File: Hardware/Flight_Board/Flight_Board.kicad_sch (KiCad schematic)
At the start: 0 parts

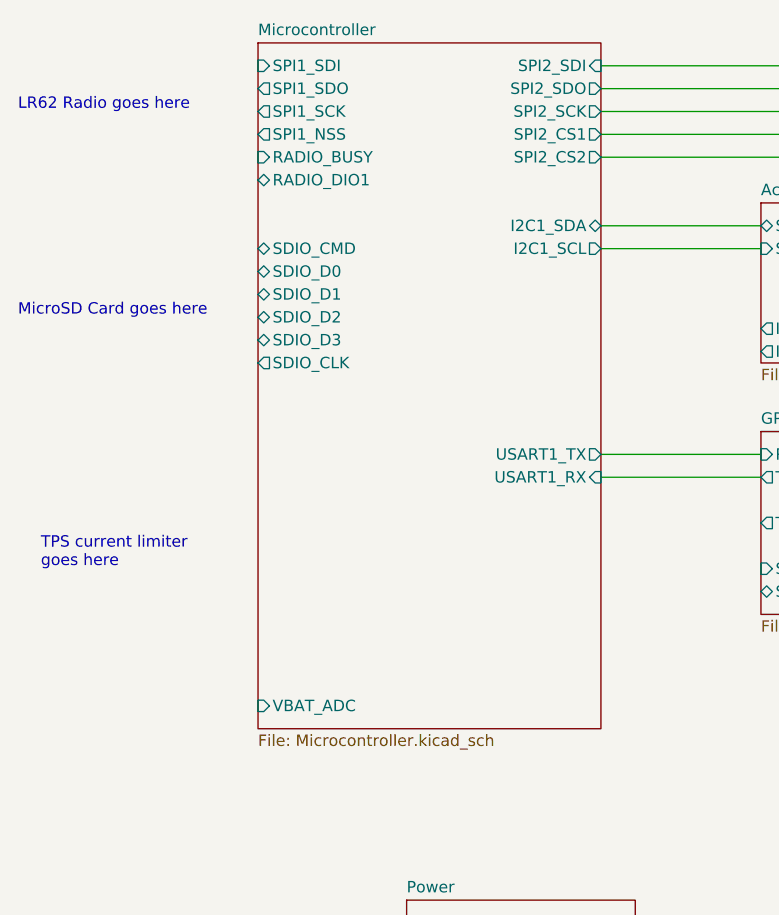
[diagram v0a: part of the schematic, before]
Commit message: add MicroSD
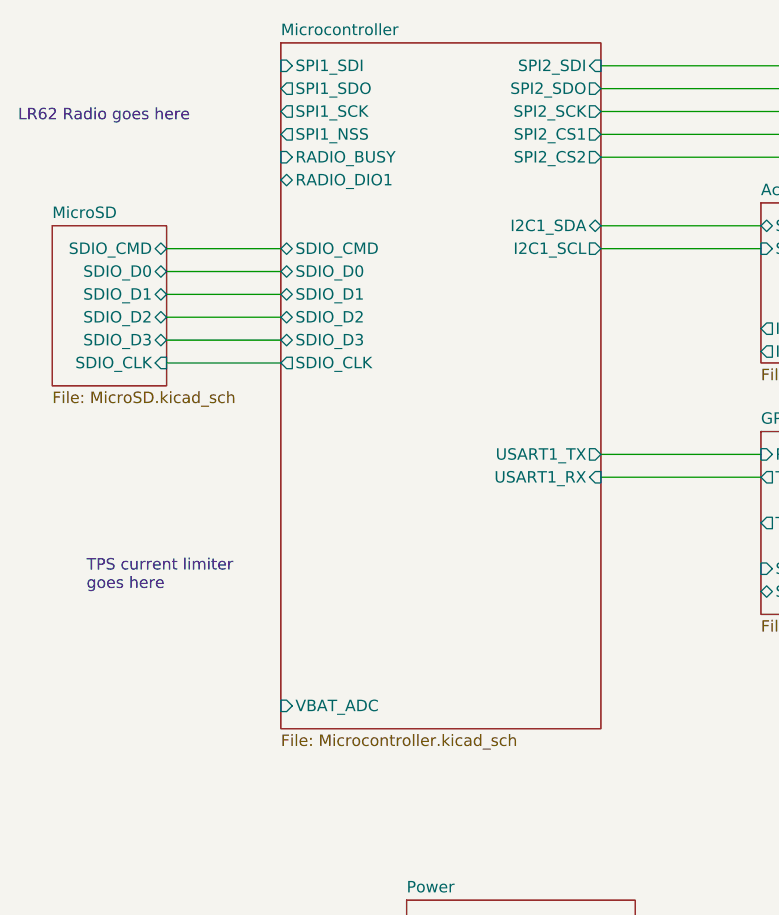
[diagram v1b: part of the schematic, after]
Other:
- added sheet MicroSD (MicroSD.kicad_sch)
- note removed: "MicroSD Card goes here"
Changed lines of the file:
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@@
+    (stroke (width 0) (type default))
+  )
+  (wire (pts (xy 127 60.96) (xy 139.7 60.96))
     (stroke (width 0) (type default))
   )
@@
     (stroke (width 0) (type default))
   )
+  (wire (pts (xy 127 68.58) (xy 139.7 68.58))
+    (stroke (width 0) (type default))
+  )
   (wire (pts (xy 233.68 68.58) (xy 238.76 68.58))
     (stroke (width 0) (type default))
@@
     (stroke (width 0) (type default))
   )
+  (wire (pts (xy 127 63.5) (xy 139.7 63.5))
+    (stroke (width 0) (type default))
+  )
   (wire (pts (xy 231.14 45.72) (xy 238.76 45.72))
     (stroke (width 0) (type default))
@@
     (stroke (width 0) (type default))
   )
+  (wire (pts (xy 127 73.66) (xy 139.7 73.66))
+    (stroke (width 0) (type default))
+  )
   (wire (pts (xy 233.68 43.18) (xy 233.68 68.58))
     (stroke (width 0) (type default))
@@
     (stroke (width 0) (type default))
   )
+  (wire (pts (xy 127 71.12) (xy 139.7 71.12))
+    (stroke (width 0) (type default))
+  )
   (wire (pts (xy 236.22 40.64) (xy 236.22 66.04))
     (stroke (width 0) (type default))
@@
     (stroke (width 0) (type default))
   )
+  (wire (pts (xy 127 66.04) (xy 139.7 66.04))
+    (stroke (width 0) (type default))
+  )
   (wire (pts (xy 175.26 58.42) (xy 193.04 58.42))
     (stroke (width 0) (type default))
@@
     (stroke (width 0) (type default))
   )
-  (text "MicroSD Card goes here" (at 110.49 68.58 0)
+  (text "TPS current limiter\ngoes here" (at 118.11 99.06 0)
     (effects (font (size 1.27 1.27)) (justify left bottom))
   )
-  (text "TPS current limiter\ngoes here" (at 113.03 96.52 0)
+  (text "LR62 Radio goes here" (at 110.49 46.99 0)
     (effects (font (size 1.27 1.27)) (justify left bottom))
   )
-  (text "LR62 Radio goes here" (at 110.49 45.72 0)
-    (effects (font (size 1.27 1.27)) (justify left bottom))
-  )
   (sheet (at 238.76 38.1) (size 12.7 17.78) (fields_autoplaced)
     (stroke (width 0.1524) (type solid))
@@
     )
   )
-  (sheet (at 137.16 38.1) (size 38.1 76.2) (fields_autoplaced)
-    (stroke (width 0.1524) (type solid))
-    (fill (color 0 0 0 0.0000))
-    (property "Sheetname" "Microcontroller" (at 137.16 37.3884 0)
-      (effects (font (size 1.27 1.27)) (justify left bottom))
-    )
-    (property "Sheetfile" "Microcontroller.kicad_sch" (at 137.16 114.8846 0)
+  (sheet (at 114.3 58.42) (size 12.7 17.78) (fields_autoplaced)
+    (stroke (width 0.1524) (type solid))
+    (fill (color 0 0 0 0.0000))
+    (property "Sheetname" "MicroSD" (at 114.3 57.7084 0)
+      (effects (font (size 1.27 1.27)) (justify left bottom))
+    )
+    (property "Sheetfile" "MicroSD.kicad_sch" (at 114.3 76.7846 0)
+      (effects (font (size 1.27 1.27)) (justify left top))
+    )
+    (pin "SDIO_D0" bidirectional (at 127 63.5 0)
+      (effects (font (size 1.27 1.27)) (justify right))
+    )
+    (pin "SDIO_D2" bidirectional (at 127 68.58 0)
+      (effects (font (size 1.27 1.27)) (justify right))
+    )
+    (pin "SDIO_D1" bidirectional (at 127 66.04 0)
+      (effects (font (size 1.27 1.27)) (justify right))
+    )
+    (pin "SDIO_D3" bidirectional (at 127 71.12 0)
+      (effects (font (size 1.27 1.27)) (justify right))
+    )
+    (pin "SDIO_CLK" input (at 127 73.66 0)
+      (effects (font (size 1.27 1.27)) (justify right))
+    )
+    (pin "SDIO_CMD" bidirectional (at 127 60.96 0)
+      (effects (font (size 1.27 1.27)) (justify right))
+    )
+    (instances
+      (project "Flight_Board"
+        (path "/e8eb85d5-f1ff-4500-895d-25b9ff5f6d36" (page "8"))
+      )
+    )
+  )
+  (sheet (at 139.7 38.1) (size 35.56 76.2) (fields_autoplaced)
+    (stroke (width 0.1524) (type solid))
+    (fill (color 0 0 0 0.0000))
+    (property "Sheetname" "Microcontroller" (at 139.7 37.3884 0)
+      (effects (font (size 1.27 1.27)) (justify left bottom))
+    )
+    (property "Sheetfile" "Microcontroller.kicad_sch" (at 139.7 114.8846 0)
       (effects (font (size 1.27 1.27)) (justify left top))
     )
@@
       (effects (font (size 1.27 1.27)) (justify right))
     )
-    (pin "SPI1_NSS" output (at 137.16 48.26 180)
-      (effects (font (size 1.27 1.27)) (justify left))
-    )
-    (pin "SPI1_SCK" output (at 137.16 45.72 180)
-      (effects (font (size 1.27 1.27)) (justify left))
-    )
-    (pin "SPI1_SDI" input (at 137.16 40.64 180)
-      (effects (font (size 1.27 1.27)) (justify left))
-    )
-    (pin "SPI1_SDO" output (at 137.16 43.18 180)
+    (pin "SPI1_NSS" output (at 139.7 48.26 180)
+      (effects (font (size 1.27 1.27)) (justify left))
+    )
+    (pin "SPI1_SCK" output (at 139.7 45.72 180)
+      (effects (font (size 1.27 1.27)) (justify left))
+    )
+    (pin "SPI1_SDI" input (at 139.7 40.64 180)
+      (effects (font (size 1.27 1.27)) (justify left))
+    )
+    (pin "SPI1_SDO" output (at 139.7 43.18 180)
       (effects (font (size 1.27 1.27)) (justify left))
     )
@@
       (effects (font (size 1.27 1.27)) (justify right))
     )
-    (pin "SDIO_CLK" output (at 137.16 73.66 180)
-      (effects (font (size 1.27 1.27)) (justify left))
-    )
-    (pin "RADIO_BUSY" input (at 137.16 50.8 180)
-      (effects (font (size 1.27 1.27)) (justify left))
-    )
-    (pin "RADIO_DIO1" bidirectional (at 137.16 53.34 180)
-      (effects (font (size 1.27 1.27)) (justify left))
-    )
-    (pin "SDIO_D3" bidirectional (at 137.16 71.12 180)
-      (effects (font (size 1.27 1.27)) (justify left))
-    )
-    (pin "SDIO_CMD" bidirectional (at 137.16 60.96 180)
-      (effects (font (size 1.27 1.27)) (justify left))
-    )
-    (pin "SDIO_D0" bidirectional (at 137.16 63.5 180)
-      (effects (font (size 1.27 1.27)) (justify left))
-    )
-    (pin "SDIO_D1" bidirectional (at 137.16 66.04 180)
-      (effects (font (size 1.27 1.27)) (justify left))
-    )
-    (pin "SDIO_D2" bidirectional (at 137.16 68.58 180)
-      (effects (font (size 1.27 1.27)) (justify left))
-    )
-    (pin "VBAT_ADC" input (at 137.16 111.76 180)
-      (effects (font (size 1.27 1.27)) (justify left))
-    )
+    (pin "SDIO_CLK" output (at 139.7 73.66 180)
+      (effects (font (size 1.27 1.27)) (justify left))
+    )
+    (pin "RADIO_BUSY" input (at 139.7 50.8 180)
+      (effects (font (size 1.27 1.27)) (justify left))
+    )
+    (pin "RADIO_DIO1" bidirectional (at 139.7 53.34 180)
+      (effects (font (size 1.27 1.27)) (justify left))
+    )
+    (pin "SDIO_D3" bidirectional (at 139.7 71.12 180)
+      (effects (font (size 1.27 1.27)) (justify left))
+    )
+    (pin "SDIO_CMD" bidirectional (at 139.7 60.96 180)
+      (effects (font (size 1.27 1.27)) (justify left))
+    )
+    (pin "SDIO_D0" bidirectional (at 139.7 63.5 180)
+      (effects (font (size 1.27 1.27)) (justify left))
+    )
+    (pin "SDIO_D1" bidirectional (at 139.7 66.04 180)
+      (effects (font (size 1.27 1.27)) (justify left))
+    )
+    (pin "SDIO_D2" bidirectional (at 139.7 68.58 180)
+      (effects (font (size 1.27 1.27)) (justify left))
+    )
+    (pin "VBAT_ADC" input (at 139.7 111.76 180)
+      (effects (font (size 1.27 1.27)) (justify left))
+    )

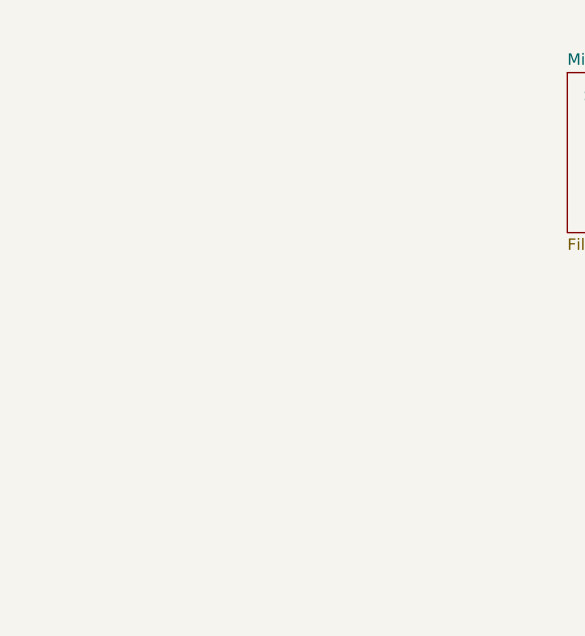
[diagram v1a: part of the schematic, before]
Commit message: make Current Switch
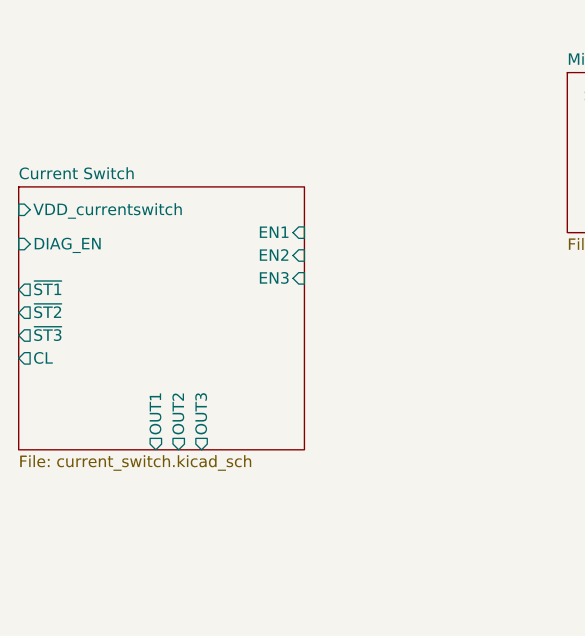
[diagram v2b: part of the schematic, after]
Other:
- added sheet Current Switch (current_switch.kicad_sch)
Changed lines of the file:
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@@
+    )
+  )
+  (sheet (at 53.34 71.12) (size 31.75 29.21) (fields_autoplaced)
+    (stroke (width 0.1524) (type solid))
+    (fill (color 0 0 0 0.0000))
+    (property "Sheetname" "Current Switch" (at 53.34 70.4084 0)
+      (effects (font (size 1.27 1.27)) (justify left bottom))
+    )
+    (property "Sheetfile" "current_switch.kicad_sch" (at 53.34 100.9146 0)
+      (effects (font (size 1.27 1.27)) (justify left top))
+    )
+    (pin "OUT3" output (at 73.66 100.33 270)
+      (effects (font (size 1.27 1.27)) (justify left))
+    )
+    (pin "OUT2" output (at 71.12 100.33 270)
+      (effects (font (size 1.27 1.27)) (justify left))
+    )
+    (pin "OUT1" output (at 68.58 100.33 270)
+      (effects (font (size 1.27 1.27)) (justify left))
+    )
+    (pin "~{ST2}" output (at 53.34 85.09 180)
+      (effects (font (size 1.27 1.27)) (justify left))
+    )
+    (pin "~{ST1}" output (at 53.34 82.55 180)
+      (effects (font (size 1.27 1.27)) (justify left))
+    )
+    (pin "~{ST3}" output (at 53.34 87.63 180)
+      (effects (font (size 1.27 1.27)) (justify left))
+    )
+    (pin "CL" output (at 53.34 90.17 180)
+      (effects (font (size 1.27 1.27)) (justify left))
+    )
+    (pin "DIAG_EN" input (at 53.34 77.47 180)
+      (effects (font (size 1.27 1.27)) (justify left))
+    )
+    (pin "VDD_currentswitch" input (at 53.34 73.66 180)
+      (effects (font (size 1.27 1.27)) (justify left))
+    )
+    (pin "EN2" input (at 85.09 78.74 0)
+      (effects (font (size 1.27 1.27)) (justify right))
+    )
+    (pin "EN1" input (at 85.09 76.2 0)
+      (effects (font (size 1.27 1.27)) (justify right))
+    )
+    (pin "EN3" input (at 85.09 81.28 0)
+      (effects (font (size 1.27 1.27)) (justify right))
+    )
+    (instances
+      (project "Flight_Board"
+        (path "/e8eb85d5-f1ff-4500-895d-25b9ff5f6d36" (page "9"))
+      )
     )
   )

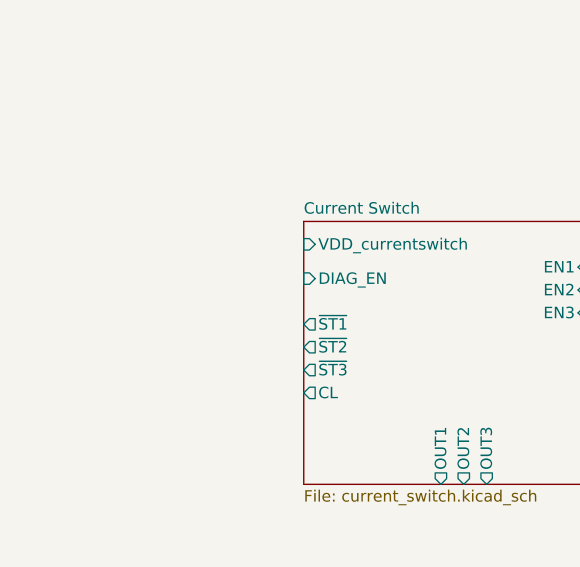
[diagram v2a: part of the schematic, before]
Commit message: remove STBar pullups
note made to toggle internal pullups on mcu to handle external pullups for diagnostic lines
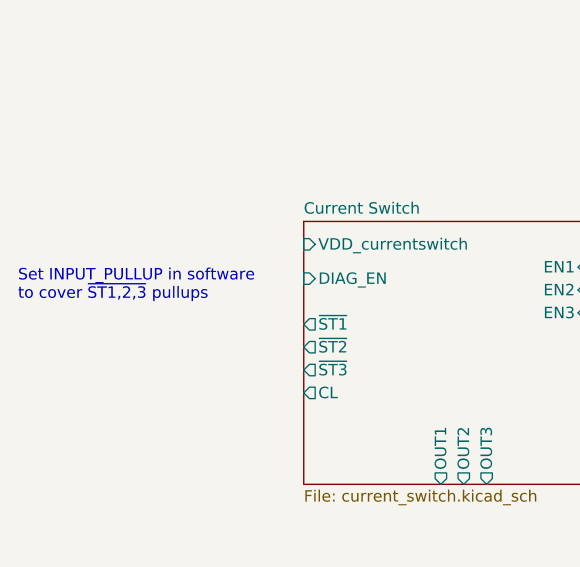
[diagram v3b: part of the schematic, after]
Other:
- note added: "Set INPUT_PULLUP in software to cover ~{ST1,2,3} pullups"
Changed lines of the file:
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@@
     (stroke (width 0) (type default))
+  )
+  (text "Set INPUT_PULLUP in software\nto cover ~{ST1,2,3} pullups\n"
+    (at 21.59 80.01 0)
+    (effects (font (size 1.27 1.27)) (justify left bottom))
   )
   (text "TPS current limiter\ngoes here" (at 118.11 99.06 0)

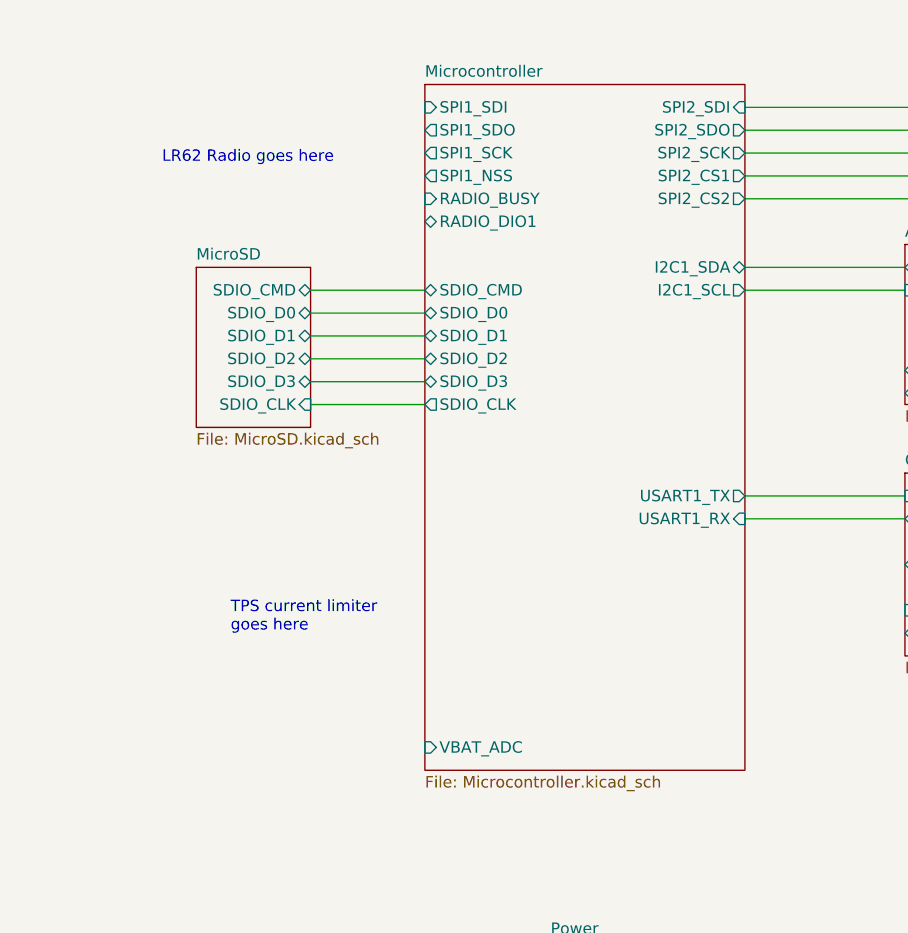
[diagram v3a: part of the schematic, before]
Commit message: Added LoRa board sheet and basic component
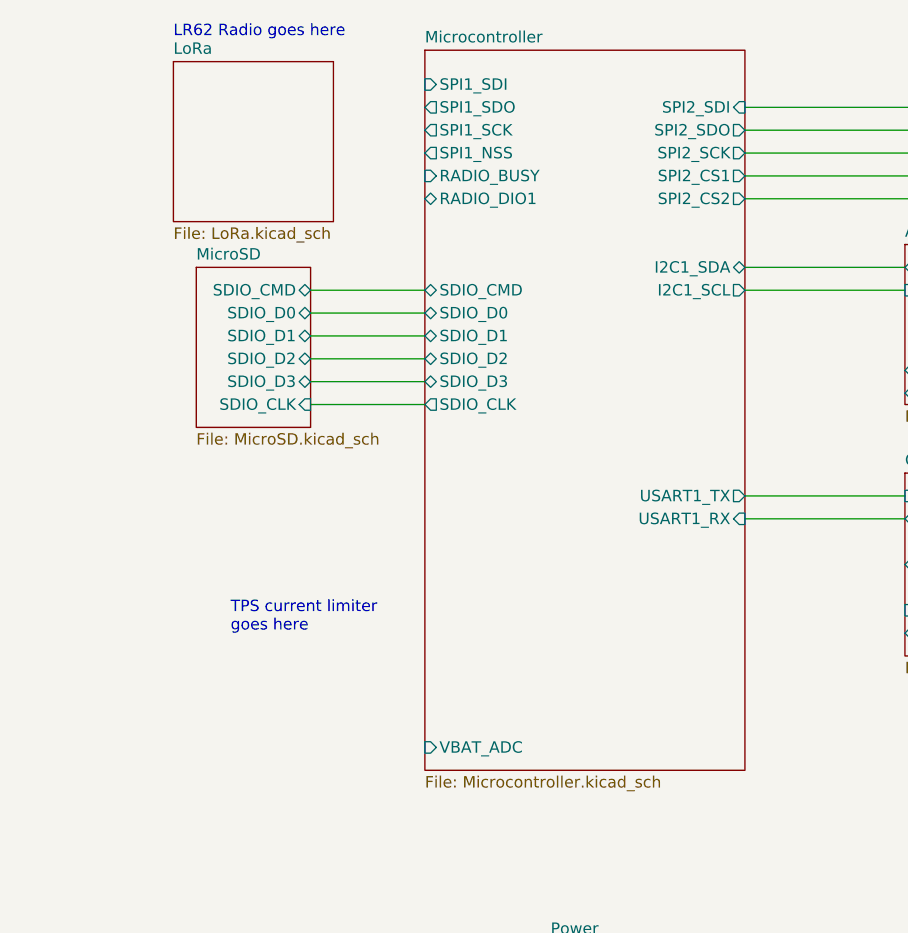
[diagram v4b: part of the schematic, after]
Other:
- added sheet LoRa (LoRa.kicad_sch)
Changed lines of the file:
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@@
     (effects (font (size 1.27 1.27)) (justify left bottom))
   )
-  (text "LR62 Radio goes here" (at 110.49 46.99 0)
+  (text "LR62 Radio goes here" (at 111.76 33.02 0)
     (effects (font (size 1.27 1.27)) (justify left bottom))
   )
@@
     )
   )
+  (sheet (at 111.76 35.56) (size 17.78 17.78) (fields_autoplaced)
+    (stroke (width 0.1524) (type solid))
+    (fill (color 0 0 0 0.0000))
+    (property "Sheetname" "LoRa" (at 111.76 34.8484 0)
+      (effects (font (size 1.27 1.27)) (justify left bottom))
+    )
+    (property "Sheetfile" "LoRa.kicad_sch" (at 111.76 53.9246 0)
+      (effects (font (size 1.27 1.27)) (justify left top))
+    )
+    (instances
+      (project "Flight_Board"
+        (path "/e8eb85d5-f1ff-4500-895d-25b9ff5f6d36" (page "10"))
+      )
+    )
+  )
   (sheet (at 53.34 71.12) (size 31.75 29.21) (fields_autoplaced)
     (stroke (width 0.1524) (type solid))
@@
     )
   )
-  (sheet (at 139.7 38.1) (size 35.56 76.2) (fields_autoplaced)
-    (stroke (width 0.1524) (type solid))
-    (fill (color 0 0 0 0.0000))
-    (property "Sheetname" "Microcontroller" (at 139.7 37.3884 0)
+  (sheet (at 139.7 34.29) (size 35.56 80.01) (fields_autoplaced)
+    (stroke (width 0.1524) (type solid))
+    (fill (color 0 0 0 0.0000))
+    (property "Sheetname" "Microcontroller" (at 139.7 33.5784 0)
       (effects (font (size 1.27 1.27)) (justify left bottom))
     )
@@
       (effects (font (size 1.27 1.27)) (justify right))
     )
-    (pin "SPI1_NSS" output (at 139.7 48.26 180)
-      (effects (font (size 1.27 1.27)) (justify left))
-    )
-    (pin "SPI1_SCK" output (at 139.7 45.72 180)
-      (effects (font (size 1.27 1.27)) (justify left))
-    )
-    (pin "SPI1_SDI" input (at 139.7 40.64 180)
-      (effects (font (size 1.27 1.27)) (justify left))
-    )
-    (pin "SPI1_SDO" output (at 139.7 43.18 180)
+    (pin "SPI1_NSS" output (at 139.7 45.72 180)
+      (effects (font (size 1.27 1.27)) (justify left))
+    )
+    (pin "SPI1_SCK" output (at 139.7 43.18 180)
+      (effects (font (size 1.27 1.27)) (justify left))
+    )
+    (pin "SPI1_SDI" input (at 139.7 38.1 180)
+      (effects (font (size 1.27 1.27)) (justify left))
+    )
+    (pin "SPI1_SDO" output (at 139.7 40.64 180)
       (effects (font (size 1.27 1.27)) (justify left))
     )
@@
       (effects (font (size 1.27 1.27)) (justify left))
     )
-    (pin "RADIO_BUSY" input (at 139.7 50.8 180)
-      (effects (font (size 1.27 1.27)) (justify left))
-    )
-    (pin "RADIO_DIO1" bidirectional (at 139.7 53.34 180)
-      (effects (font (size 1.27 1.27)) (justify left))
-    )
+    (pin "RADIO_BUSY" input (at 139.7 48.26 180)
+      (effects (font (size 1.27 1.27)) (justify left))
+    )
+    (pin "RADIO_DIO1" bidirectional (at 139.7 50.8 180)
+      (effects (font (size 1.27 1.27)) (justify left))
+    )
